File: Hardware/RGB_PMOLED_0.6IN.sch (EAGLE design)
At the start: 22 parts, among them Q1 310mA/60V/1.6Ω, U1 UG-6464TDDBG01, U2 AP3012, U3 3.3V, U4 TXB0104

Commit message: Intemediate commit
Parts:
- added C3: 1.0uF, SparkFun-Capacitors:1.0UF-0603-16V-10%
- added C7: 2.2uF/25V, SparkFun-Capacitors:2.2UF-0805-25V-(+80/-20%)
- added R5: 390k, SparkFun-Resistors:390KOHM-0603-1/10W-1%
- C2: value 1.0uF/25V -> 1.0uF; device SparkFun-Capacitors:1.0UF-0805-25V-(+80/-20%) -> SparkFun-Capacitors:1.0UF-0603-16V-10%
- U1: value UG-6464TDDBG01 -> UG-6464TDDBG01-EXT; device RGB_OLED:UG-6464TDDBG01 -> RGB_OLED:UG-6464TDDBG01-EXT
- renumbered C10 to C5, C11 to C6, C9 to C4
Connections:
- removed net N$12: U1.VSS
- removed net N$8: U1.VCC
- removed net N$9: U1.VCOMH
- new net N$5: C7.2, U1.VCOMH
- net 12V: now also U1.VCC
- net GND: now also C3.2, C7.1, R5.1, U1.VSS
- net N$10: now also C8.1
- net N$11: now also R5.2
- net VIN: now also C3.1; no longer C8.1
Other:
- note added: "!RES! Will tend to be pulled high by this logic level shifter. It is up to an external device to pull it low to reset the screen"
- note added: "Connector"
- note added: "Normally I'd connect Vdd to 3.3V but in the datasheet the maximum is listed as 2.75V - this is an output from an internal power supply"
- note added: "RGB PMOLED 0.6""
- note added: "TO 3.3V???"
- note added: "The resistor between Iref and VSS is chosen as 330k ohm because the datasheet says to keep the current to 10 uA at maximum. However this is based on an assumption that the voltage at Iref will be fixed at 3.3V"
- moved on the sheet: C1, C2, C8, D1, J1, L1, R1, R2, U1, U2

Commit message: First revision
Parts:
- added H1, H2: STAND-OFF, SparkFun-Hardware:STAND-OFF
- added LOGO2: OSHW-LOGOS, SparkFun-Aesthetics:OSHW-LOGOS
- C7: value 2.2uF/25V -> 2.2uF
- U1: value UG-6464TDDBG01-EXT -> UG-6464TDDBG01-FLD; device RGB_OLED:UG-6464TDDBG01-EXT -> RGB_OLED:UG-6464TDDBG01-FLD
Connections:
- removed net !CS!: U4.A4
- net !CS: now also U4.A1
- net !CS!_HIGH: now also J1.7, U4.B1; no longer J1.4, U4.B4
- net D/!C!_HIGH: now also J1.6; no longer J1.5
- net GND: now also C7.2; no longer C7.1
- net N$5: now also C7.1; no longer C7.2
- net SCLK_HIGH: now also J1.5; no longer J1.6
- net SDIN: now also U4.A4; no longer U4.A1
- net SDIN_HIGH: now also J1.4, U4.B4; no longer J1.7, U4.B1
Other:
- moved on the sheet: C7

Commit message: Panelized and gerberified
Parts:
- added FD3, FD4: FIDUCIAL1X2, SparkFun-Aesthetics:FIDUCIAL1X2
- added R6: 10k, SparkFun-Resistors:10KOHM-0603-1/10W-1%
- L1: device 1.81_Greyscale_OLED_Breakout:INDUCTORINDUCTOR_10UH -> SparkFun-Coils:INDUCTORINDUCTOR_10UH
- U2: device 1.81_Greyscale_OLED_Breakout:AP3012 -> SparkFun-IC-Power:AP3012
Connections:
- removed net N$10: C8.1, U1.VDD
- net !CS: now also R6.1
- net 3.3V: now also C8.1, R6.2, U1.VDD
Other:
- note added: "CS Pullup"
- note added: "X01"
- note removed: "TO 3.3V???"
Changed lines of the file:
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@@
 <parts>
 <part name="FRAME1" library="SparkFun-Aesthetics" deviceset="FRAME-LETTER" device=""/>
-<part name="U2" library="1.81_Greyscale_OLED_Breakout" deviceset="AP3012" device=""/>
+<part name="U2" library="SparkFun-IC-Power" deviceset="AP3012" device="" value="AP3012"/>
 <part name="C1" library="SparkFun-Capacitors" deviceset="1.0UF" device="-0603-16V-10%" value="1.0uF"/>
 <part name="R1" library="SparkFun-Resistors" deviceset="47KOHM" device="-0603-1/10W-1%" value="47k"/>
 <part name="R2" library="SparkFun-Resistors" deviceset="5.6KOHM" device="-0603-1/10W-1%" value="5.6k"/>
 <part name="D1" library="SparkFun-DiscreteSemi" deviceset="DIODE-SCHOTTKY" device="-BAT20J" value="1A/23V/620mV"/>
-<part name="L1" library="1.81_Greyscale_OLED_Breakout" deviceset="INDUCTOR" device="INDUCTOR_10UH" value="10uH"/>
 <part name="SUPPLY1" library="SparkFun-PowerSymbols" deviceset="VIN" device=""/>
 <part name="GND1" library="SparkFun-PowerSymbols" deviceset="GND" device=""/>
@@
 <part name="H1" library="SparkFun-Hardware" deviceset="STAND-OFF" device="" value="STAND-OFF"/>
 <part name="H2" library="SparkFun-Hardware" deviceset="STAND-OFF" device="" value="STAND-OFF"/>
+<part name="SUPPLY12" library="SparkFun-PowerSymbols" deviceset="3.3V" device=""/>
+<part name="R6" library="SparkFun-Resistors" deviceset="10KOHM" device="-0603-1/10W-1%" value="10k"/>
+<part name="SUPPLY15" library="SparkFun-PowerSymbols" deviceset="3.3V" device=""/>
+<part name="FD3" library="SparkFun-Aesthetics" deviceset="FIDUCIAL" device="1X2"/>
+<part name="FD4" library="SparkFun-Aesthetics" deviceset="FIDUCIAL" device="1X2"/>
+<part name="L1" library="SparkFun-Coils" deviceset="INDUCTOR" device="INDUCTOR_10UH" value="10uH"/>
 </parts>
 <sheets>
@@
 <text x="5.08" y="111.76" size="2.54" layer="94">RGB PMOLED 0.6"</text>
 <text x="7.62" y="40.64" size="2.54" layer="94">Connector</text>
-<text x="38.1" y="93.98" size="1.27" layer="97" rot="R90">TO 3.3V???</text>
+<text x="238.76" y="7.62" size="2.54" layer="94">X01</text>
+<text x="162.56" y="96.52" size="2.54" layer="94">CS Pullup</text>
 </plain>
 <instances>
@@
 <instance part="R2" gate="G$1" x="121.92" y="144.78" rot="R90"/>
 <instance part="D1" gate="G$1" x="114.3" y="167.64" rot="MR180"/>
-<instance part="L1" gate="G$1" x="96.52" y="167.64" rot="R90"/>
 <instance part="SUPPLY1" gate="G$1" x="76.2" y="160.02"/>
 <instance part="GND1" gate="1" x="83.82" y="142.24"/>
@@
 <instance part="H1" gate="G$1" x="241.3" y="25.4"/>
 <instance part="H2" gate="G$1" x="238.76" y="27.94"/>
+<instance part="SUPPLY12" gate="G$1" x="35.56" y="93.98"/>
+<instance part="R6" gate="G$1" x="170.18" y="81.28" rot="R90"/>
+<instance part="SUPPLY15" gate="G$1" x="170.18" y="88.9"/>
+<instance part="FD3" gate="G$1" x="243.84" y="33.02"/>
+<instance part="FD4" gate="G$1" x="246.38" y="30.48"/>
+<instance part="L1" gate="G$1" x="96.52" y="167.64" rot="R90"/>
 </instances>
 <busses>
@@
 <wire x1="81.28" y1="157.48" x2="81.28" y2="167.64" width="0.1524" layer="91"/>
 <junction x="81.28" y="157.48"/>
+<wire x1="81.28" y1="167.64" x2="91.44" y2="167.64" width="0.1524" layer="91"/>
 <pinref part="L1" gate="G$1" pin="1"/>
-<wire x1="81.28" y1="167.64" x2="91.44" y2="167.64" width="0.1524" layer="91"/>
 </segment>
 <segment>
@@
 <net name="N$2" class="0">
 <segment>
-<pinref part="L1" gate="G$1" pin="2"/>
 <pinref part="D1" gate="G$1" pin="A"/>
 <wire x1="101.6" y1="167.64" x2="109.22" y2="167.64" width="0.1524" layer="91"/>
@@
 <wire x1="109.22" y1="157.48" x2="109.22" y2="167.64" width="0.1524" layer="91"/>
 <junction x="109.22" y="167.64"/>
+<pinref part="L1" gate="G$1" pin="2"/>
 </segment>
 </net>
@@
 <junction x="205.74" y="91.44"/>
 </segment>
+<segment>
+<pinref part="U1" gate="G$1" pin="VDD"/>
+<wire x1="63.5" y1="78.74" x2="40.64" y2="78.74" width="0.1524" layer="91"/>
+<wire x1="40.64" y1="78.74" x2="40.64" y2="86.36" width="0.1524" layer="91"/>
+<wire x1="40.64" y1="86.36" x2="35.56" y2="86.36" width="0.1524" layer="91"/>
+<pinref part="C8" gate="G$1" pin="1"/>
+<wire x1="35.56" y1="86.36" x2="35.56" y2="83.82" width="0.1524" layer="91"/>
+<wire x1="35.56" y1="86.36" x2="35.56" y2="93.98" width="0.1524" layer="91"/>
+<junction x="35.56" y="86.36"/>
+<pinref part="SUPPLY12" gate="G$1" pin="3.3V"/>
+</segment>
+<segment>
+<pinref part="R6" gate="G$1" pin="2"/>
+<pinref part="SUPPLY15" gate="G$1" pin="3.3V"/>
+<wire x1="170.18" y1="86.36" x2="170.18" y2="88.9" width="0.1524" layer="91"/>
+</segment>
 </net>
 <net name="D/!C" class="0">
@@
 <wire x1="200.66" y1="127" x2="198.12" y2="127" width="0.1524" layer="91"/>
 <label x="198.12" y="127" size="1.27" layer="95" rot="R180" xref="yes"/>
+</segment>
+<segment>
+<pinref part="R6" gate="G$1" pin="1"/>
+<wire x1="170.18" y1="73.66" x2="170.18" y2="76.2" width="0.1524" layer="91"/>
+<label x="170.18" y="73.66" size="1.27" layer="95" rot="R270" xref="yes"/>
 </segment>
 </net>
@@
 </segment>
 </net>
-<net name="N$10" class="0">
-<segment>
-<pinref part="U1" gate="G$1" pin="VDD"/>
-<wire x1="63.5" y1="78.74" x2="40.64" y2="78.74" width="0.1524" layer="91"/>
-<wire x1="40.64" y1="78.74" x2="40.64" y2="86.36" width="0.1524" layer="91"/>
-<wire x1="40.64" y1="86.36" x2="35.56" y2="86.36" width="0.1524" layer="91"/>
-<pinref part="C8" gate="G$1" pin="1"/>
-<wire x1="35.56" y1="86.36" x2="35.56" y2="83.82" width="0.1524" layer="91"/>
-<wire x1="35.56" y1="86.36" x2="35.56" y2="96.52" width="0.1524" layer="91"/>
-<junction x="35.56" y="86.36"/>
-</segment>
-</net>

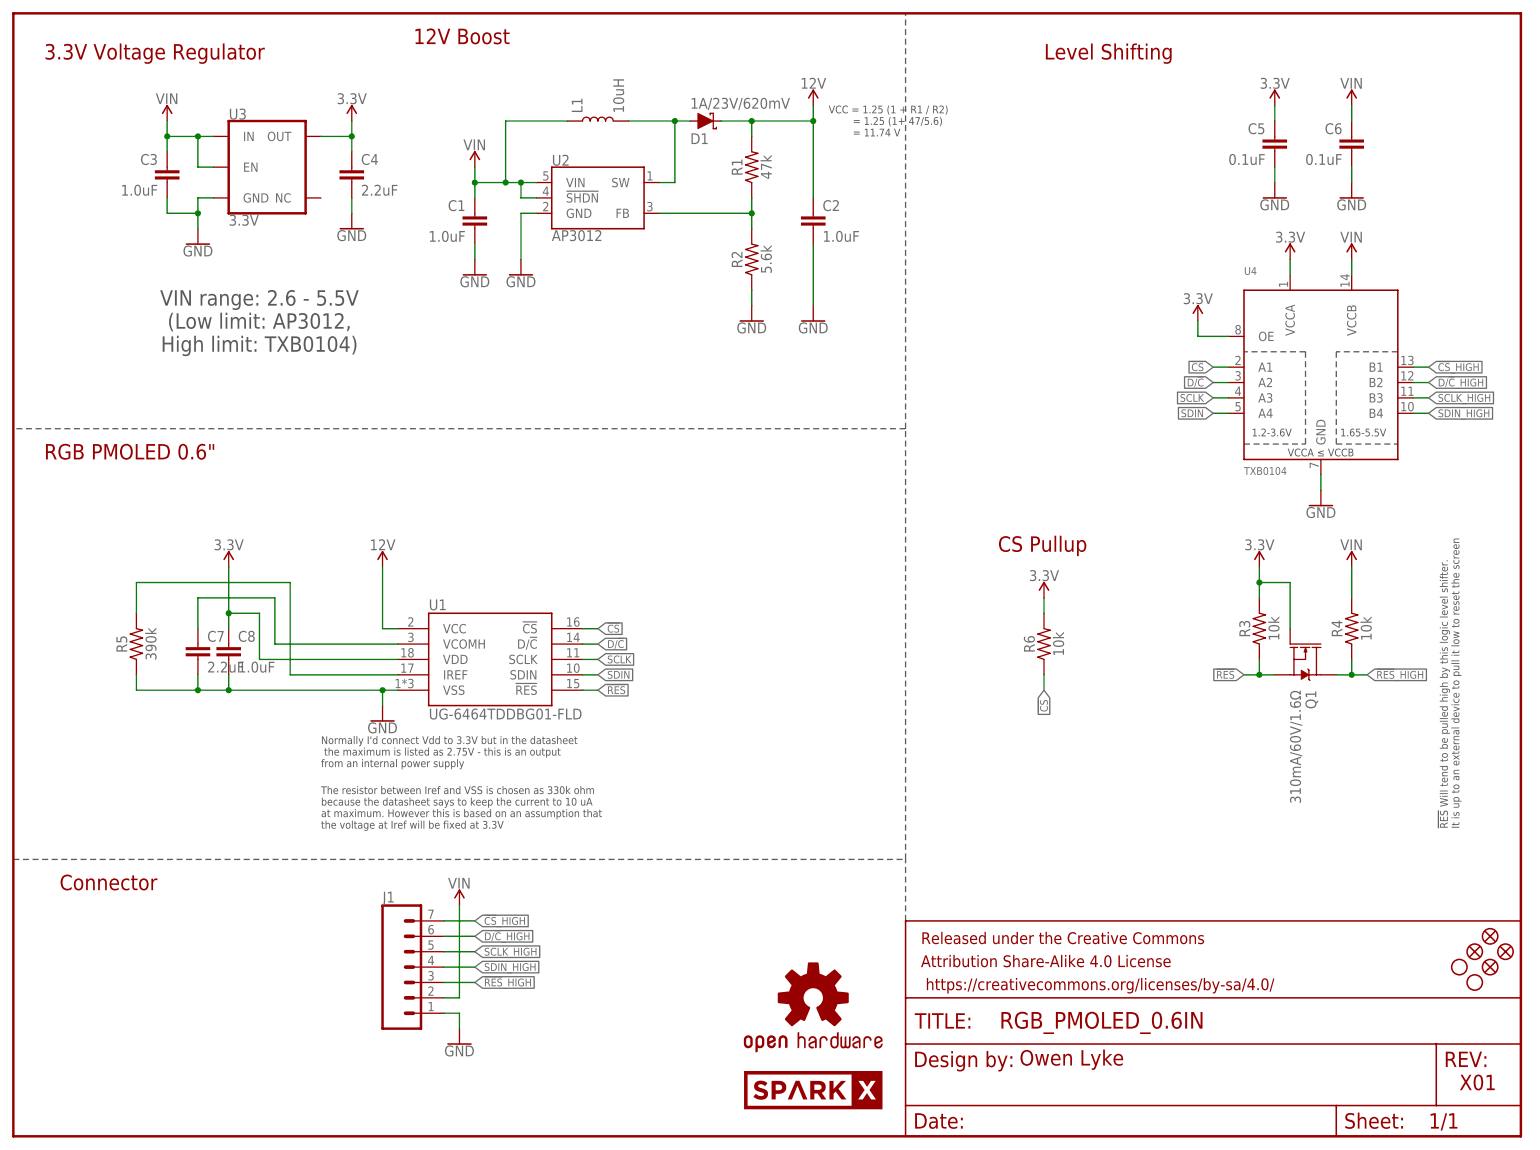
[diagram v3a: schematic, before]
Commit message: Revision 2 of board using a connector
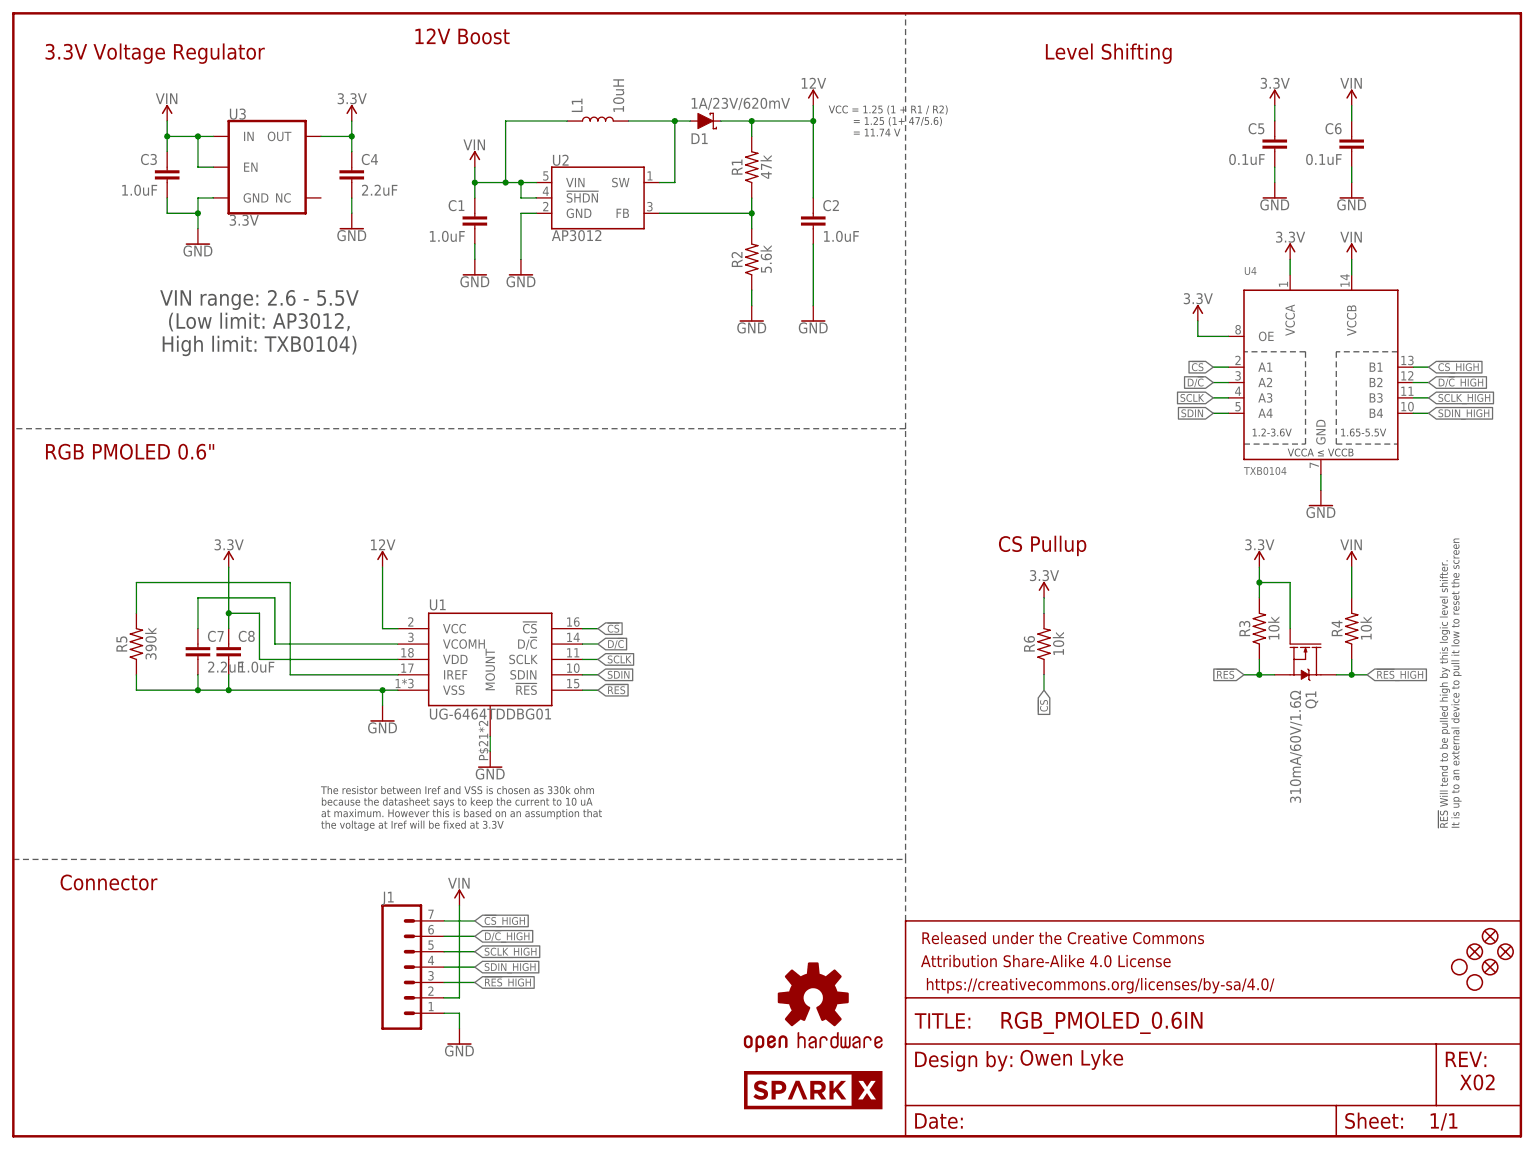
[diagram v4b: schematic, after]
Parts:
- L1: device SparkFun-Coils:INDUCTORINDUCTOR_10UH -> SparkFun-Coils:INDUCTOR-CDRH-10UH
- U1: value UG-6464TDDBG01-FLD -> UG-6464TDDBG01; device RGB_OLED:UG-6464TDDBG01-FLD -> RGB_OLED:UG-6464TDDBG01
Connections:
- net GND: now also U1.MOUNT
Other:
- note added: "X02"
- note removed: "Normally I'd connect Vdd to 3.3V but in the datasheet the maximum is listed as 2.75V - this is an output from an internal power supply"
- note removed: "X01"
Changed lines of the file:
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@@
 <part name="GND6" library="SparkFun-PowerSymbols" deviceset="GND" device=""/>
 <part name="R5" library="SparkFun-Resistors" deviceset="390KOHM" device="-0603-1/10W-1%" value="390k"/>
-<part name="U1" library="RGB_OLED" deviceset="UG-6464TDDBG01" device="-FLD" value="UG-6464TDDBG01-FLD"/>
+<part name="U1" library="RGB_OLED" deviceset="UG-6464TDDBG01" device="" value="UG-6464TDDBG01"/>
 <part name="C8" library="SparkFun-Capacitors" deviceset="1.0UF" device="-0603-16V-10%" value="1.0uF"/>
 <part name="C2" library="SparkFun-Capacitors" deviceset="1.0UF" device="-0603-16V-10%" value="1.0uF"/>
@@
 <part name="FD3" library="SparkFun-Aesthetics" deviceset="FIDUCIAL" device="1X2"/>
 <part name="FD4" library="SparkFun-Aesthetics" deviceset="FIDUCIAL" device="1X2"/>
-<part name="L1" library="SparkFun-Coils" deviceset="INDUCTOR" device="INDUCTOR_10UH" value="10uH"/>
+<part name="L1" library="SparkFun-Coils" deviceset="INDUCTOR" device="-CDRH-10UH" value="10uH"/>
+<part name="GND7" library="SparkFun-PowerSymbols" deviceset="GND" device=""/>
 </parts>
 <sheets>
@@
 <text x="238.76" y="50.8" size="1.27" layer="97" rot="R90">!RES! Will tend to be pulled high by this logic level shifter.
 It is up to an external device to pull it low to reset the screen</text>
-<text x="50.8" y="60.96" size="1.27" layer="97">Normally I'd connect Vdd to 3.3V but in the datasheet
- the maximum is listed as 2.75V - this is an output
-from an internal power supply</text>
 <text x="50.8" y="50.8" size="1.27" layer="97">The resistor between Iref and VSS is chosen as 330k ohm
 because the datasheet says to keep the current to 10 uA
@@
 <text x="5.08" y="111.76" size="2.54" layer="94">RGB PMOLED 0.6"</text>
 <text x="7.62" y="40.64" size="2.54" layer="94">Connector</text>
-<text x="238.76" y="7.62" size="2.54" layer="94">X01</text>
+<text x="238.76" y="7.62" size="2.54" layer="94">X02</text>
 <text x="162.56" y="96.52" size="2.54" layer="94">CS Pullup</text>
 </plain>
@@
 <instance part="FD4" gate="G$1" x="246.38" y="30.48"/>
 <instance part="L1" gate="G$1" x="96.52" y="167.64" rot="R90"/>
+<instance part="GND7" gate="1" x="78.74" y="60.96"/>
 </instances>
 <busses>
@@
 <pinref part="C7" gate="G$1" pin="2"/>
 </segment>
+<segment>
+<pinref part="U1" gate="G$1" pin="MOUNT"/>
+<pinref part="GND7" gate="1" pin="GND"/>
+<wire x1="78.74" y1="66.04" x2="78.74" y2="63.5" width="0.1524" layer="91"/>
+</segment>
 </net>
